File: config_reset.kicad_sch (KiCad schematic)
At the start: 22 parts, among them U1 NX1H35 PBGA625, U6 M95P32-IXMNT/E, Y2 LFSPXO025225_25MHz

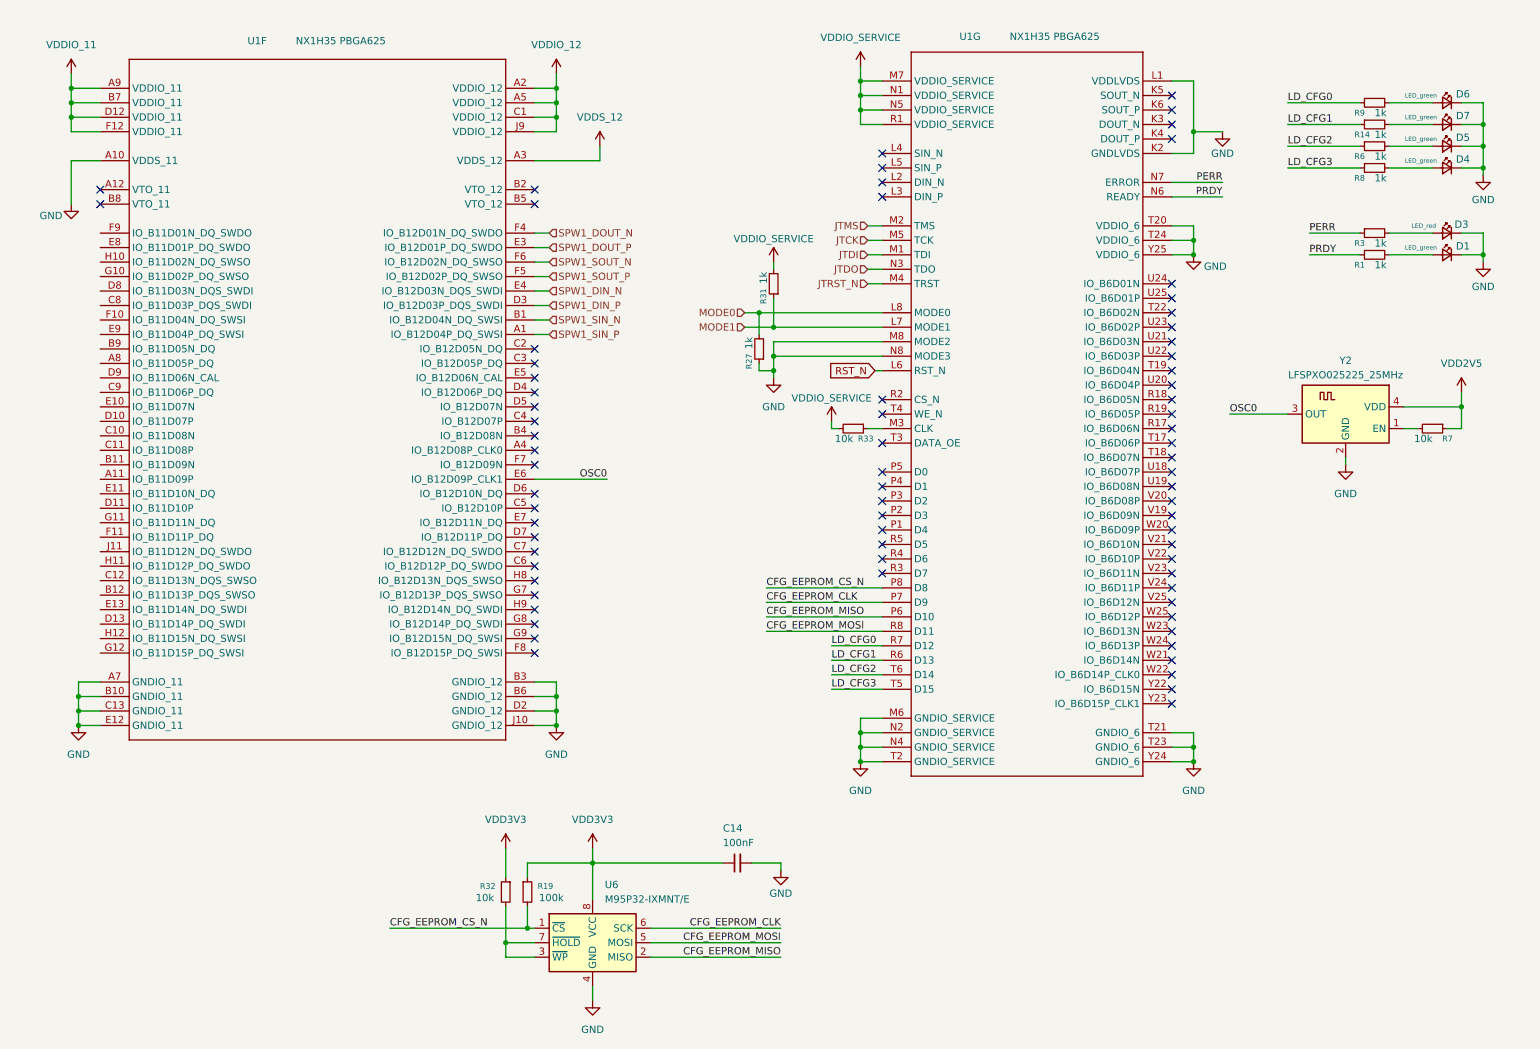
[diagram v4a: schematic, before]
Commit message: CFG, bga sdram, banks to connectors, docoupling
Finished completely routing bga sdram, finished tracing Banks to connectors DF9. Finished tracing Picoblade, diode, reset supervisor. Finished tracing LEDS on bank 5. Finished decoupling all banks and core. Missing only the power tree and power rail level decoupling.
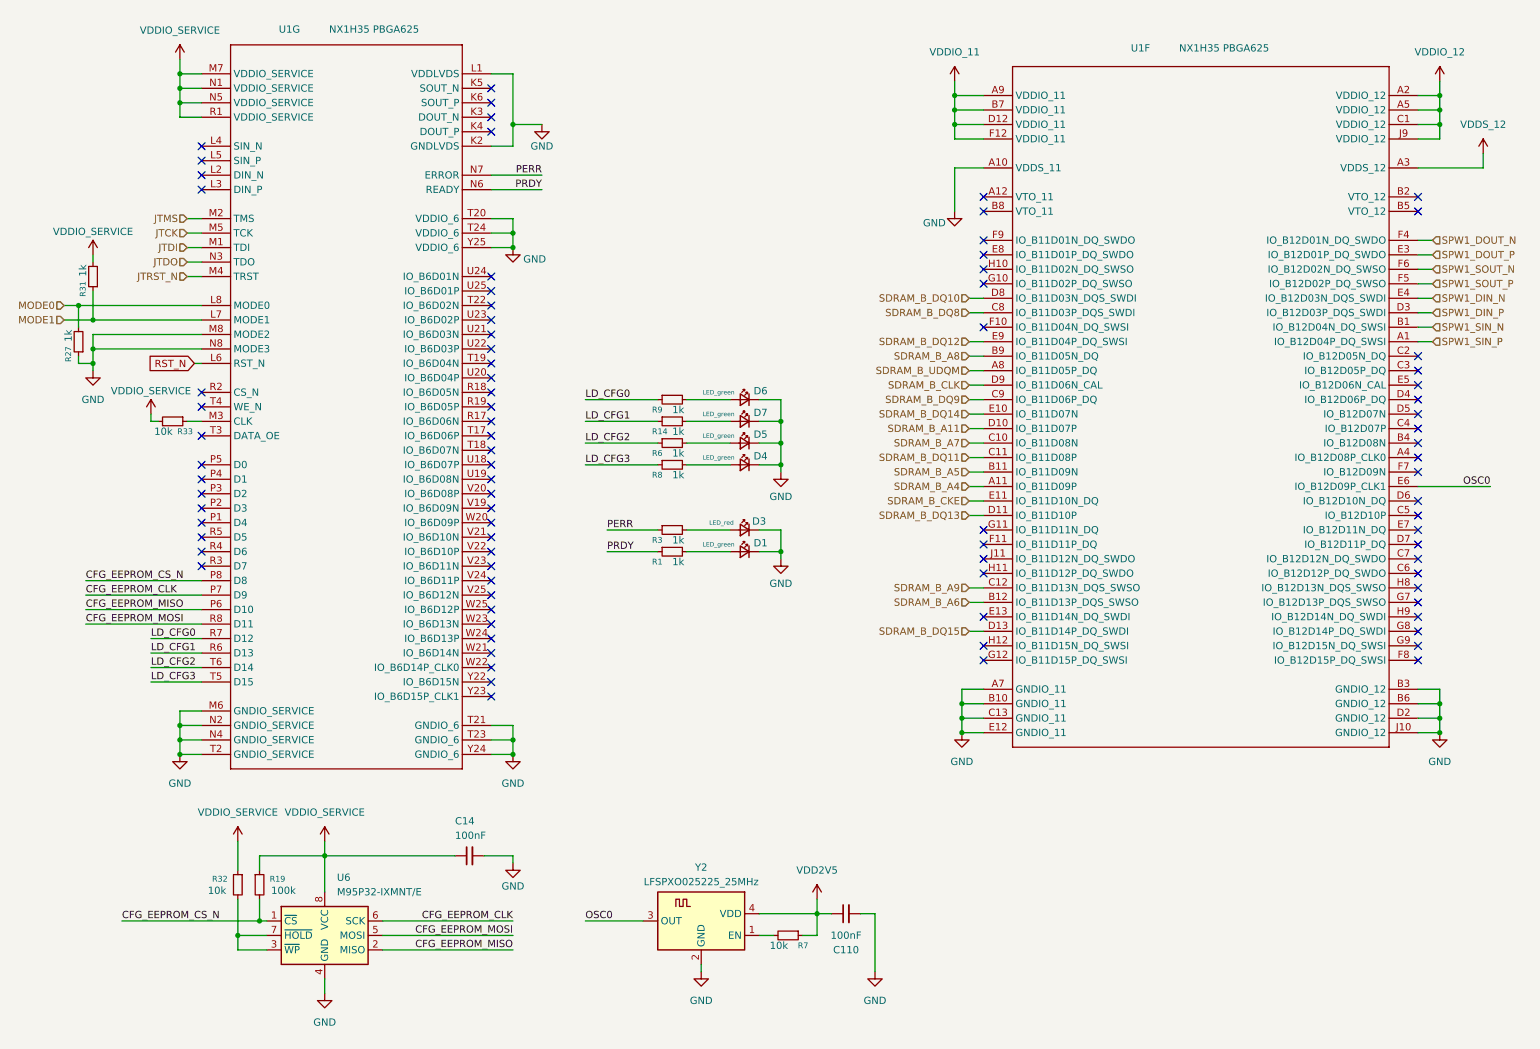
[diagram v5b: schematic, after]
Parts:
- added C110: 100nF, Capacitor_SMD:C_0402_1005Metric_Pad0.74x0.62mm_HandSolder, symbol Device:C_Small
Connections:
- net VDD3V3 is gone; now on net VDDIO_SERVICE: C14.1, R19.1, R32.1, U6.8 (VCC)
- net GND: now also C110.2
- net VDD2V5: now also C110.1
- net SDRAM_B_A4: now reaches U1.A11 (IO_B11D09P)
- net SDRAM_B_UDQM: now reaches U1.A8 (IO_B11D05P_DQ)
- net SDRAM_B_A5: now reaches U1.B11 (IO_B11D09N)
- net SDRAM_B_A6: now reaches U1.B12 (IO_B11D13P_DQS_SWSO)
- net SDRAM_B_A8: now reaches U1.B9 (IO_B11D05N_DQ)
- net SDRAM_B_A7: now reaches U1.C10 (IO_B11D08N)
- net SDRAM_B_DQ11: now reaches U1.C11 (IO_B11D08P)
- net SDRAM_B_A9: now reaches U1.C12 (IO_B11D13N_DQS_SWSO)
- net SDRAM_B_DQ8: now reaches U1.C8 (IO_B11D03P_DQS_SWDI)
- net SDRAM_B_DQ9: now reaches U1.C9 (IO_B11D06P_DQ)
- net SDRAM_B_A11: now reaches U1.D10 (IO_B11D07P)
- net SDRAM_B_DQ13: now reaches U1.D11 (IO_B11D10P)
- net SDRAM_B_DQ15: now reaches U1.D13 (IO_B11D14P_DQ_SWDI)
- net SDRAM_B_DQ10: now reaches U1.D8 (IO_B11D03N_DQS_SWDI)
- net SDRAM_B_CLK: now reaches U1.D9 (IO_B11D06N_CAL)
- net SDRAM_B_DQ14: now reaches U1.E10 (IO_B11D07N)
- net SDRAM_B_CKE: now reaches U1.E11 (IO_B11D10N_DQ)
- net SDRAM_B_DQ12: now reaches U1.E9 (IO_B11D04P_DQ_SWSI)
- no-connect marks 74 -> 86
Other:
- moved on the sheet: C14, D1, D3, D4, D5, D6, D7, R1, R14, R19, R27, R3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

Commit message: power tree
power tree defined. Few changes remaining but almost finalized
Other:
- moved on the sheet: R32
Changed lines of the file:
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@@
 	)
 	(junction
+		(at 58.42 176.53)
+		(diameter 0)
+		(color 0 0 0 0)
+	)
+	(junction
 		(at 180.34 36.83)
 		(diameter 0)
@@
 	)
 	(junction
-		(at 58.42 176.53)
+		(at 265.43 34.29)
 		(diameter 0)
 		(color 0 0 0 0)
 	)
 	(junction
-		(at 265.43 34.29)
+		(at 265.43 31.75)
 		(diameter 0)
 		(color 0 0 0 0)
 	)
 	(junction
-		(at 265.43 31.75)
+		(at 52.07 179.07)
 		(diameter 0)
 		(color 0 0 0 0)
@@
 	)
 	(junction
-		(at 54.61 179.07)
-		(diameter 0)
-		(color 0 0 0 0)
-	)
-	(junction
 		(at 149.86 111.76)
 		(diameter 0)
@@
 	(wire
 		(pts
-			(xy 54.61 172.72) (xy 54.61 179.07)
+			(xy 52.07 171.45) (xy 52.07 179.07)
 		)
 		(stroke
@@
 	(wire
 		(pts
-			(xy 59.69 179.07) (xy 54.61 179.07)
-		)
-		(stroke
-			(width 0)
-			(type default)
-		)
-	)
-	(wire
-		(pts
 			(xy 185.42 118.11) (xy 182.88 118.11)
 		)
@@
 	(wire
 		(pts
-			(xy 54.61 181.61) (xy 59.69 181.61)
-		)
-		(stroke
-			(width 0)
-			(type default)
-		)
-	)
-	(wire
-		(pts
 			(xy 181.61 138.43) (xy 185.42 138.43)
 		)
@@
 	(wire
 		(pts
+			(xy 52.07 162.56) (xy 52.07 166.37)
+		)
+		(stroke
+			(width 0)
+			(type default)
+		)
+	)
+	(wire
+		(pts
 			(xy 44.45 35.56) (xy 48.26 35.56)
 		)
@@
 	(wire
 		(pts
+			(xy 52.07 179.07) (xy 59.69 179.07)
+		)
+		(stroke
+			(width 0)
+			(type default)
+		)
+	)
+	(wire
+		(pts
 			(xy 44.45 144.78) (xy 44.45 147.32)
 		)
@@
 	(wire
 		(pts
+			(xy 52.07 181.61) (xy 59.69 181.61)
+		)
+		(stroke
+			(width 0)
+			(type default)
+		)
+	)
+	(wire
+		(pts
 			(xy 39.37 127) (xy 48.26 127)
 		)
@@
 	(wire
 		(pts
-			(xy 54.61 162.56) (xy 54.61 167.64)
+			(xy 149.86 85.09) (xy 149.86 88.9)
 		)
 		(stroke
@@
 	(wire
 		(pts
-			(xy 149.86 85.09) (xy 149.86 88.9)
+			(xy 52.07 179.07) (xy 52.07 181.61)
 		)
 		(stroke
@@
 	(wire
 		(pts
-			(xy 34.29 176.53) (xy 58.42 176.53)
+			(xy 31.75 176.53) (xy 58.42 176.53)
 		)
 		(stroke
@@
 	(wire
 		(pts
-			(xy 54.61 179.07) (xy 54.61 181.61)
-		)
-		(stroke
-			(width 0)
-			(type default)
-		)
-	)
-	(wire
-		(pts
 			(xy 45.72 53.34) (xy 48.26 53.34)
 		)
@@
 	)
 	(label "CFG_EEPROM_CS_N"
-		(at 34.29 176.53 0)
+		(at 31.75 176.53 0)
 		(effects
 			(font
@@
 	(symbol
 		(lib_id "DataHub_PWR_symbols:VDDIO_SERVICE")
-		(at 54.61 162.56 0)
+		(at 52.07 162.56 0)
 		(unit 1)
 		(exclude_from_sim no)
@@
 		(fields_autoplaced yes)
 		(property "Reference" "#PWR070"
-			(at 38.608 157.48 0)
+			(at 36.068 157.48 0)
 			(effects
 				(font
@@
 		)
 		(property "Value" "VDDIO_SERVICE"
-			(at 54.61 157.48 0)
+			(at 52.07 157.48 0)
 			(effects
 				(font
@@
 		)
 		(property "Footprint" ""
-			(at 54.61 162.56 0)
+			(at 52.07 162.56 0)
 			(effects
 				(font
@@
 		)
 		(property "Datasheet" ""
-			(at 54.61 162.56 0)
+			(at 52.07 162.56 0)
 			(effects
 				(font
@@
 		)
 		(property "Description" "Power symbol creates a global label with name \"VDDIO_SERVICE\""
-			(at 52.578 153.162 0)
+			(at 50.038 153.162 0)
 			(effects
 				(font
@@
 	(symbol
 		(lib_id "Device:R_Small")
-		(at 54.61 170.18 0)
+		(at 52.07 168.91 0)
 		(mirror y)
 		(unit 1)
@@
 		(dnp no)
 		(property "Reference" "R32"
-			(at 52.832 169.164 0)
+			(at 50.292 167.894 0)
 			(effects
 				(font
@@
 		)
 		(property "Value" "10k"
-			(at 52.578 171.196 0)
+			(at 50.038 169.926 0)
 			(effects
 				(font
@@
 		)
 		(property "Footprint" "Resistor_SMD:R_0402_1005Metric_Pad0.72x0.64mm_HandSolder"
-			(at 54.61 170.18 0)
+			(at 52.07 168.91 0)
 			(effects
 				(font
@@
 		)
 		(property "Datasheet" "~"
-			(at 54.61 170.18 0)
+			(at 52.07 168.91 0)
 			(effects
 				(font
@@
 		)
 		(property "Description" "Resistor, small symbol"
-			(at 54.61 170.18 0)
+			(at 52.07 168.91 0)
 			(effects
 				(font

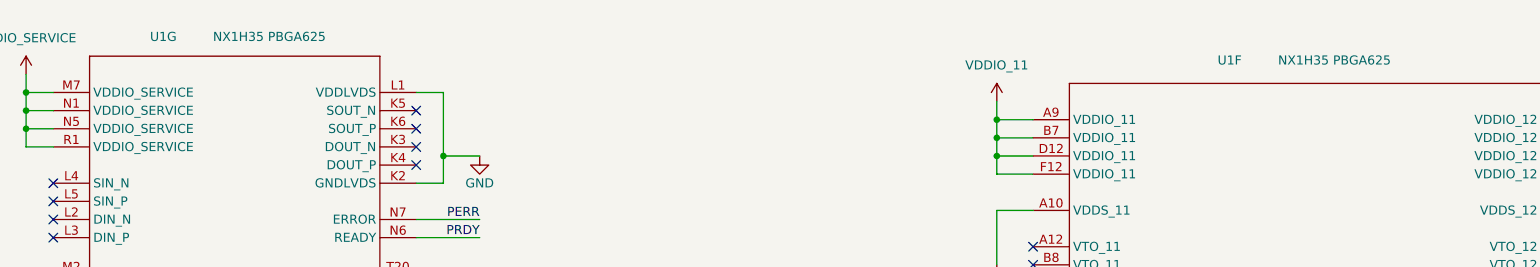
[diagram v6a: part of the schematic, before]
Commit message: finished
power planes, decoupling, ERC, DRC
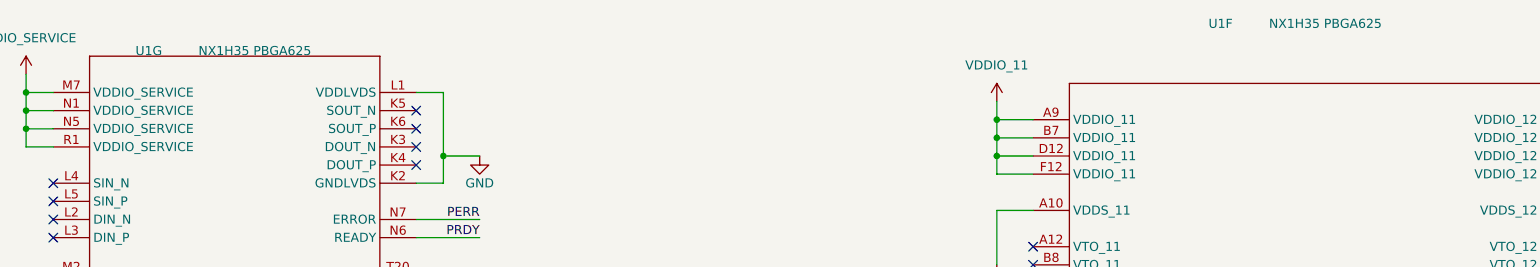
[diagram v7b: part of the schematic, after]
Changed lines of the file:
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@@
 	)
 	(symbol
+		(lib_name "root_0_BRAVE625A_Brave625.SchLib_1")
 		(lib_id "Brave625:root_0_BRAVE625A_Brave625.SchLib")
 		(at 73.66 83.82 0)
@@
 		(dnp no)
 		(property "Reference" "U1"
-			(at 65.532 20.8788 0)
+			(at 63.5 22.86 0)
 			(effects
 				(font
@@
 		)
 		(property "Value" "NX1H35 PBGA625"
-			(at 70.612 20.8788 0)
+			(at 68.58 22.86 0)
 			(effects
 				(font
@@
 		)
 		(instances
-			(project "PCB_Project"
+			(project ""
+				(path "/ae14ff2f-b8e3-4dd1-9329-e73906805e39/77861c37-88e9-4408-9723-ec14cfd3d63b"
+					(reference "U1")
+					(unit 7)
+				)
 				(path "/ae14ff2f-b8e3-4dd1-9329-e73906805e39/e4b4090a-9491-4976-8b45-759656425e5b"
 					(reference "U1")
@@
 		(dnp no)
 		(property "Reference" "U1"
-			(at 214.63 24.1808 0)
+			(at 213.36 19.05 0)
 			(effects
 				(font
@@
 		)
 		(property "Value" "NX1H35 PBGA625"
-			(at 219.71 24.1808 0)
+			(at 218.44 19.05 0)
 			(effects
 				(font
@@
 		)
 		(instances
-			(project "PCB_Project"
+			(project ""
+				(path "/ae14ff2f-b8e3-4dd1-9329-e73906805e39/77861c37-88e9-4408-9723-ec14cfd3d63b"
+					(reference "U1")
+					(unit 6)
+				)
 				(path "/ae14ff2f-b8e3-4dd1-9329-e73906805e39/e4b4090a-9491-4976-8b45-759656425e5b"
 					(reference "U1")
